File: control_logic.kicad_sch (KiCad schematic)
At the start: 60 parts, among them J12 SWD Header, J17 TC2050, SW1 KMR721NGLFS, SW2 KMR721NGLFS, U10 L7805, U11 MCP2562-E-SN, U12 STM32F105RCTx, U13 AZ1117I-3.3, U15 TPD4E1U06, Y3 8MHz 12pF

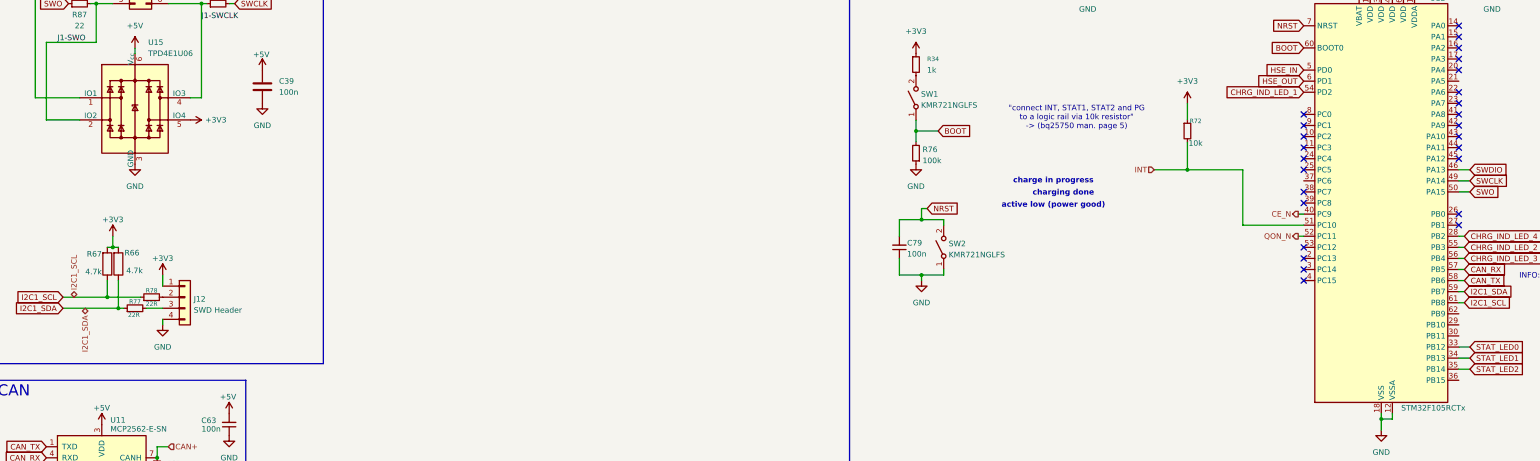
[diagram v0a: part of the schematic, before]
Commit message: finalized new balancer layout (removed R_SNS and implemented the resulting consequences); removed charger shipping mode
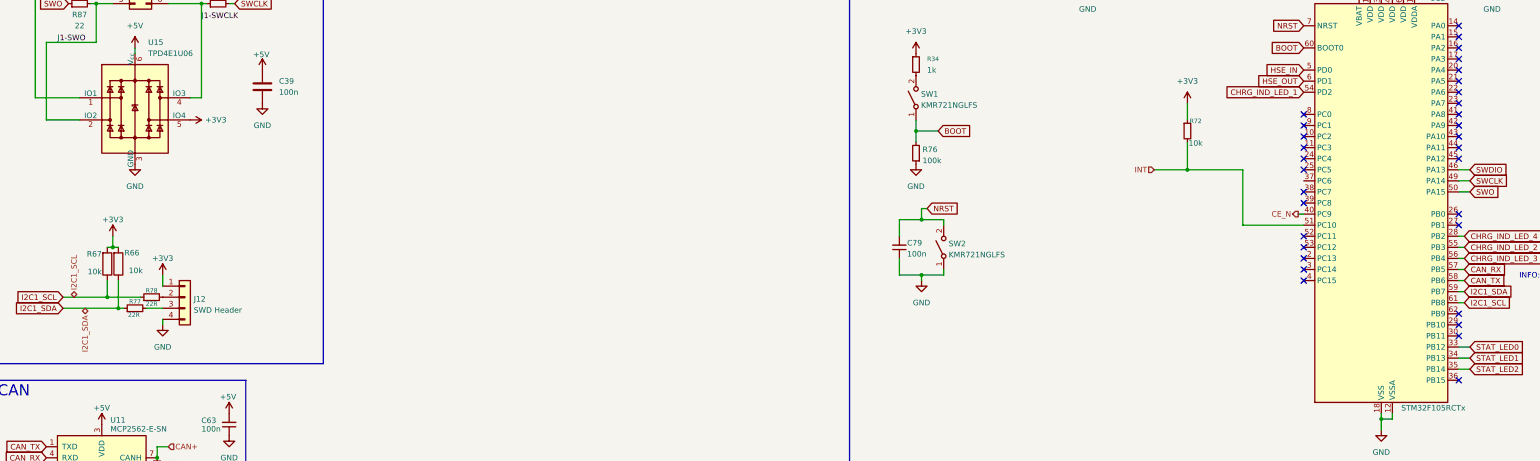
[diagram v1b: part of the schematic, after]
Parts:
- R66, R67: value 4.7k -> 10k
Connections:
- net QON_N: no longer names the net of U12.52 (PC11)
- no-connect marks 26 -> 32
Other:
- note removed: ""connect INT, STAT1, STAT2 and PG to a logic rail via 10k resistor" -> (bq25750 man. page 5)"
- note removed: "active low (power good)"
- note removed: "charge in progress"
- note removed: "charging done"
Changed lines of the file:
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@@
 		)
 	)
-	(text "\"connect INT, STAT1, STAT2 and PG \nto a logic rail via 10k resistor\" \n-> (bq25750 man. page 5)"
-		(exclude_from_sim no)
-		(at 262.89 66.802 0)
-		(effects
-			(font
-				(size 1.27 1.27)
-			)
-		)
-	)
 	(text "Charge Indicator LEDs"
 		(exclude_from_sim no)
@@
 		)
 	)
-	(text "active low (power good)"
-		(exclude_from_sim no)
-		(at 257.556 86.868 0)
-		(effects
-			(font
-				(size 1.27 1.27)
-				(thickness 0.254)
-				(bold yes)
-			)
-		)
-	)
-	(text "charge in progress"
-		(exclude_from_sim no)
-		(at 257.556 81.28 0)
-		(effects
-			(font
-				(size 1.27 1.27)
-				(thickness 0.254)
-				(bold yes)
-			)
-		)
-	)
-	(text "charging done"
-		(exclude_from_sim no)
-		(at 259.842 84.074 0)
-		(effects
-			(font
-				(size 1.27 1.27)
-				(thickness 0.254)
-				(bold yes)
-			)
-		)
-	)
 	(text "DNP"
 		(exclude_from_sim no)
@@
 	)
 	(no_connect
+		(at 350.52 58.42)
+	)
+	(no_connect
+		(at 314.96 93.98)
+	)
+	(no_connect
 		(at 314.96 86.36)
 	)
@@
 	)
 	(no_connect
+		(at 350.52 111.76)
+	)
+	(no_connect
 		(at 314.96 78.74)
 	)
@@
 	)
 	(no_connect
+		(at 350.52 114.3)
+	)
+	(no_connect
 		(at 314.96 73.66)
 	)
@@
 	)
 	(no_connect
+		(at 350.52 127)
+	)
+	(no_connect
+		(at 350.52 116.84)
+	)
+	(no_connect
 		(at 314.96 96.52)
 	)
@@
 	(wire
 		(pts
-			(xy 313.69 93.98) (xy 314.96 93.98)
-		)
-		(stroke
-			(width 0)
-			(type default)
-		)
-	)
-	(wire
-		(pts
 			(xy 384.81 222.25) (xy 384.81 229.87)
 		)
@@
 		)
 	)
-	(hierarchical_label "QON_N"
-		(shape output)
-		(at 313.69 93.98 180)
-		(effects
-			(font
-				(size 1.27 1.27)
-			)
-			(justify right)
-		)
-	)
 	(hierarchical_label "I2C1_SDA"
 		(shape bidirectional)
@@
 			)
 		)
-		(property "Value" "4.7k"
+		(property "Value" "10k"
 			(at 48.768 101.854 0)
 			(effects
@@
 			)
 		)
-		(property "Value" "4.7k"
+		(property "Value" "10k"
 			(at 39.37 102.108 0)
 			(effects

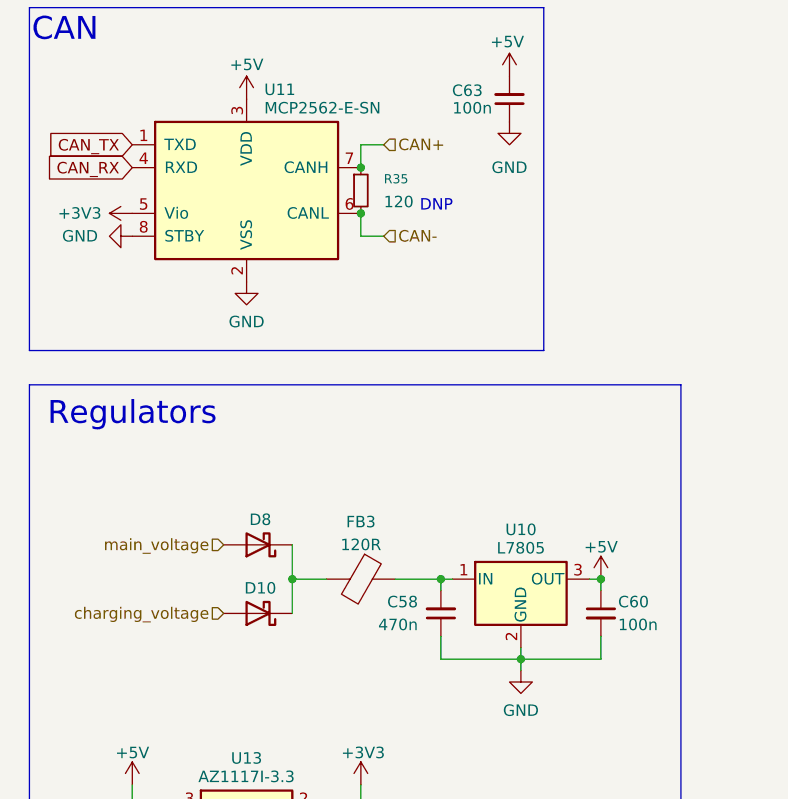
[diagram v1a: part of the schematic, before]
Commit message: implemented changes according to errors found in the schematic design review (wip)
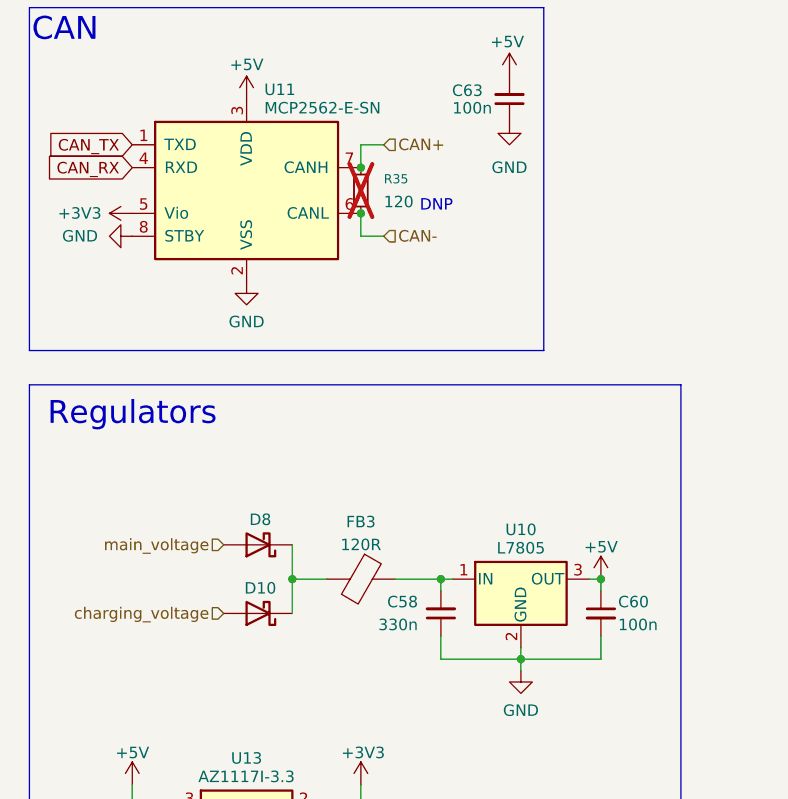
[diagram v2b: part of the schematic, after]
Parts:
- C58: value 470n -> 330n
- R35: now not fitted
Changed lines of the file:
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@@
 			)
 		)
-		(property "Value" "470n"
+		(property "Value" "330n"
 			(at 58.42 195.58 0)
 			(effects
@@
 		(in_bom yes)
 		(on_board yes)
-		(dnp no)
+		(dnp yes)
 		(fields_autoplaced yes)
 		(property "Reference" "R35"

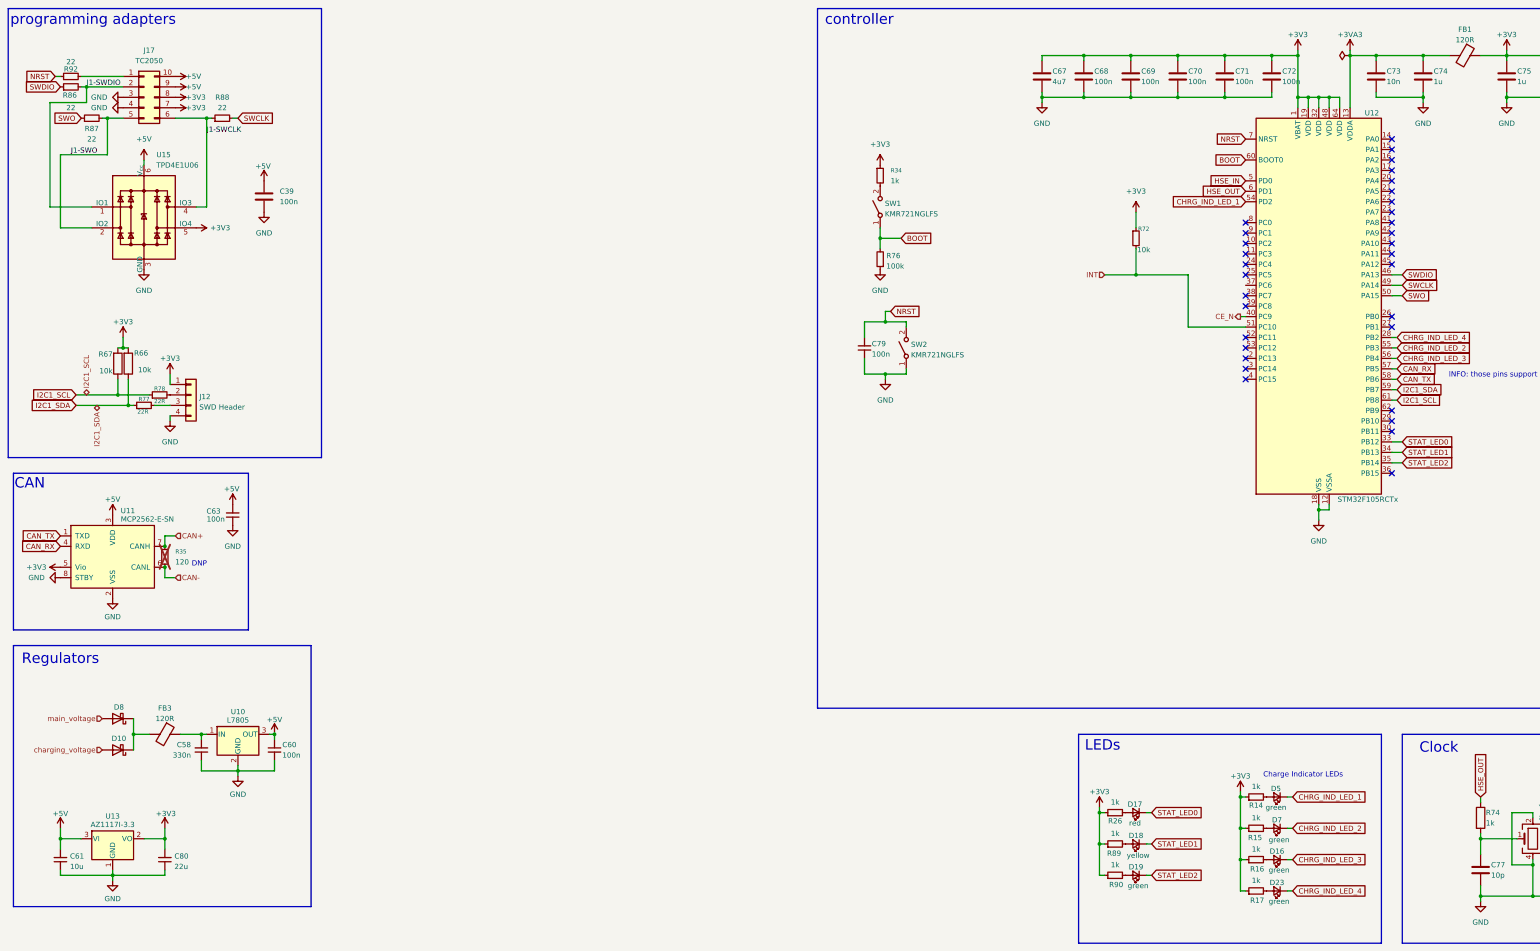
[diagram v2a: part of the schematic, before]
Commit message: added missing footprints and validated all lcsc numbers; started pcb-layouting
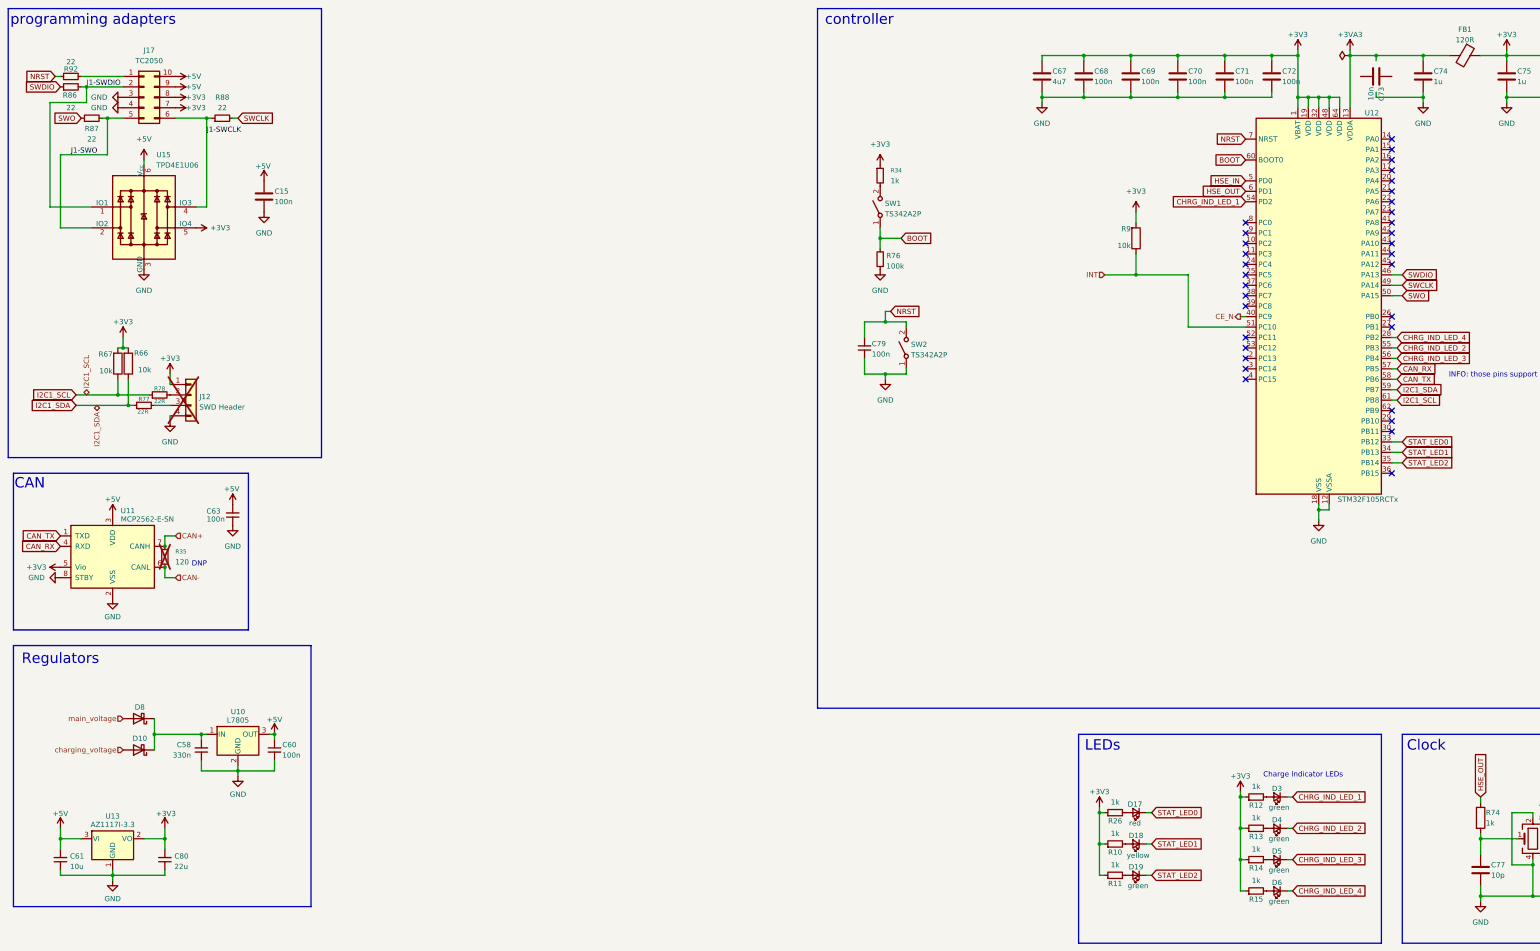
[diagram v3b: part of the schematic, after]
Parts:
- removed C39: 100n, symbol Device:C
- removed D16, D23, D7: green, LED_SMD:LED_0603_1608Metric, symbol Device:LED_Small
- removed FB3: 120R, Inductor_SMD:L_0805_2012Metric, symbol Device:FerriteBead
- removed R16, R17: 1k, Resistor_SMD:R_0603_1608Metric, symbol Device:R_Small
- removed R72: 10k, Resistor_SMD:R_0603_1608Metric, symbol Device:R_Small
- removed R89, R90: 1k, Resistor_SMD:R_0402_1005Metric, symbol Device:R_Small
- added C15: 100n, Capacitor_SMD:C_0402_1005Metric, symbol Device:C
- added D3, D4, D6: green, LED_SMD:LED_0805_2012Metric, symbol Device:LED_Small
- added R10, R11, R12, R13: 1k, Resistor_SMD:R_0402_1005Metric, symbol Device:R_Small
- added R9: 10k, Resistor_SMD:R_0402_1005Metric, symbol Device:R
- C58: LCSC (none) -> C1615; LCSC# C1623 -> (none)
- C60, C63, C69, C70, C71, C72: LCSC (none) -> C307331; LCSC# C307331 -> (none)
- C61: LCSC (none) -> C13585; LCSC# C13585 -> (none)
- C67: LCSC (none) -> C368809; LCSC# C368809 -> (none)
- C73, C76: LCSC (none) -> C60133; LCSC# C60133 -> (none)
- C74, C75: LCSC (none) -> C52923; LCSC# C52923 -> (none)
- C77, C78: LCSC (none) -> C76946; LCSC# C76946 -> (none)
- C80: LCSC (none) -> C12891; LCSC# C12891 -> (none)
- D18, D19: footprint LED_SMD:LED_0603_1608Metric -> LED_SMD:LED_0805_2012Metric
- D5: footprint LED_SMD:LED_0603_1608Metric -> LED_SMD:LED_0805_2012Metric; LCSC C2286 -> C2297
- FB1: LCSC (none) -> C14709; LCSC# C14709 -> (none)
- J12: DigiKey# N/A -> (none); LCSC (none) -> x; LCSC# N/A -> (none); Manufacturer N/A -> (none); Part# N/A -> (none); now not fitted
- J17: LCSC (none) -> x
- R14, R15: footprint Resistor_SMD:R_0603_1608Metric -> Resistor_SMD:R_0402_1005Metric
- R34: footprint Resistor_SMD:R_0603_1608Metric -> Resistor_SMD:R_0402_1005Metric; LCSC (none) -> C11702
- R66: LCSC (none) -> C25744
- R67: LCSC C105871 -> C25744
- R74: LCSC (none) -> C11702; LCSC# C21190 -> (none)
- SW1, SW2: value KMR721NGLFS -> TS342A2P; footprint Button_Switch_SMD:SW_Push_1P1T_NO_CK_KMR2 -> Button_Switch_SMD:SW_Push_SPST_NO_Alps_SKRK; LCSC C2911418 -> C5373431; Manufacturer C&K -> (none); Part# KMR721NGLFS -> (none)
- U10: LCSC (none) -> C58069; LCSC# C58069 -> (none)
- U11: LCSC (none) -> C191417; LCSC# C191417 -> (none)
- U13: LCSC (none) -> C92102; LCSC# C92102 -> (none)
- Y3: LCSC (none) -> C2149245; LCSC# C2149245 -> (none)
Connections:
- net +3V3: now also R10.1, R11.1, R12.1, R13.1, R9.2
- net +3VA3: no longer C73.1
- net +5V: now also C15.1
- net CHRG_IND_LED_1: now also D3.1 (K); no longer D5.1 (K)
- net CHRG_IND_LED_2: now also D4.1 (K)
- net CHRG_IND_LED_3: now also D5.1 (K)
- net CHRG_IND_LED_4: now also D6.1 (K)
- net GND: now also C15.2; no longer C73.2
- net INT: now also R9.1
- net at R15.2: now also D6.2 (A)
- net at D18.2 (A): now also R10.2
- net at C58.2, U10.1 (IN): now also D10.1 (K), D8.1 (K)
- net at D19.2 (A): now also R11.2
- new net: D4.2 (A), R13.2
- new net: D3.2 (A), R12.2
- no-connect marks 32 -> 33
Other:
- moved on the sheet: C73, D10, D8

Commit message: started routing Please enter the commit message for your changes. Lines starting
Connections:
- net +3VA3: now also C73.1
- net GND: now also C73.2
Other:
- moved on the sheet: C73
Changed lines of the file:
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@@
 	(symbol
 		(lib_id "Device:C")
-		(at 346.71 30.48 270)
+		(at 346.71 30.48 0)
 		(unit 1)
 		(exclude_from_sim no)
@@
 		(dnp no)
 		(property "Reference" "C73"
-			(at 347.98 33.02 0)
+			(at 349.25 29.21 0)
 			(effects
 				(font
@@
 		)
 		(property "Value" "10n"
-			(at 345.44 33.02 0)
+			(at 349.25 31.75 0)
 			(effects
 				(font
@@
 		)
 		(property "Footprint" "Capacitor_SMD:C_0402_1005Metric"
-			(at 342.9 31.4452 0)
+			(at 347.6752 34.29 0)
 			(effects
 				(font
